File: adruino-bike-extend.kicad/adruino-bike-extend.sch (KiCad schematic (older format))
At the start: 1 part

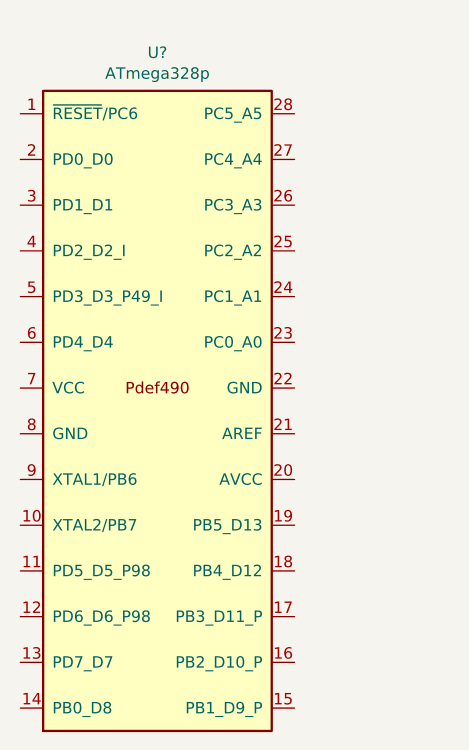
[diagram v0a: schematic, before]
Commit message: FIX - fix project library-scheme-connection
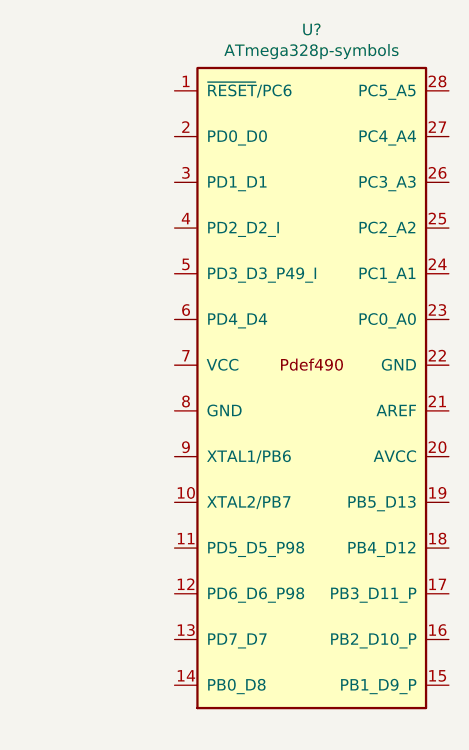
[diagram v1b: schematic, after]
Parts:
- removed U?: ATmega328p, symbol symbols:ATmega328p
- added U?: ATmega328p-symbols, symbol adruino-bike-extend-rescue:ATmega328p-symbols
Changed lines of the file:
@@
 $EndDescr
 $Comp
-L symbols:ATmega328p U?
-U 1 1 617C5F39
-P 2225 2900
-F 0 "U?" H 2225 4467 50  0000 C CNN
-F 1 "ATmega328p" H 2225 4376 50  0000 C CNN
-F 2 "" H 2225 2900 50  0001 C CNN
-F 3 "" H 2225 2900 50  0001 C CNN
-	1    2225 2900
+L adruino-bike-extend-rescue:ATmega328p-symbols U?
+U 1 1 617C6158
+P 2900 2800
+F 0 "U?" H 2900 4367 50  0000 C CNN
+F 1 "ATmega328p-symbols" H 2900 4276 50  0000 C CNN
+F 2 "" H 2900 2800 50  0001 C CNN
+F 3 "" H 2900 2800 50  0001 C CNN
+	1    2900 2800
 	1    0    0    -1
 $EndComp
